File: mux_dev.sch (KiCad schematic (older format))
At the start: 3 parts, among them U10 FSUSB42MUX, U11 FSUSB42MUX, U9 FSUSB42MUX

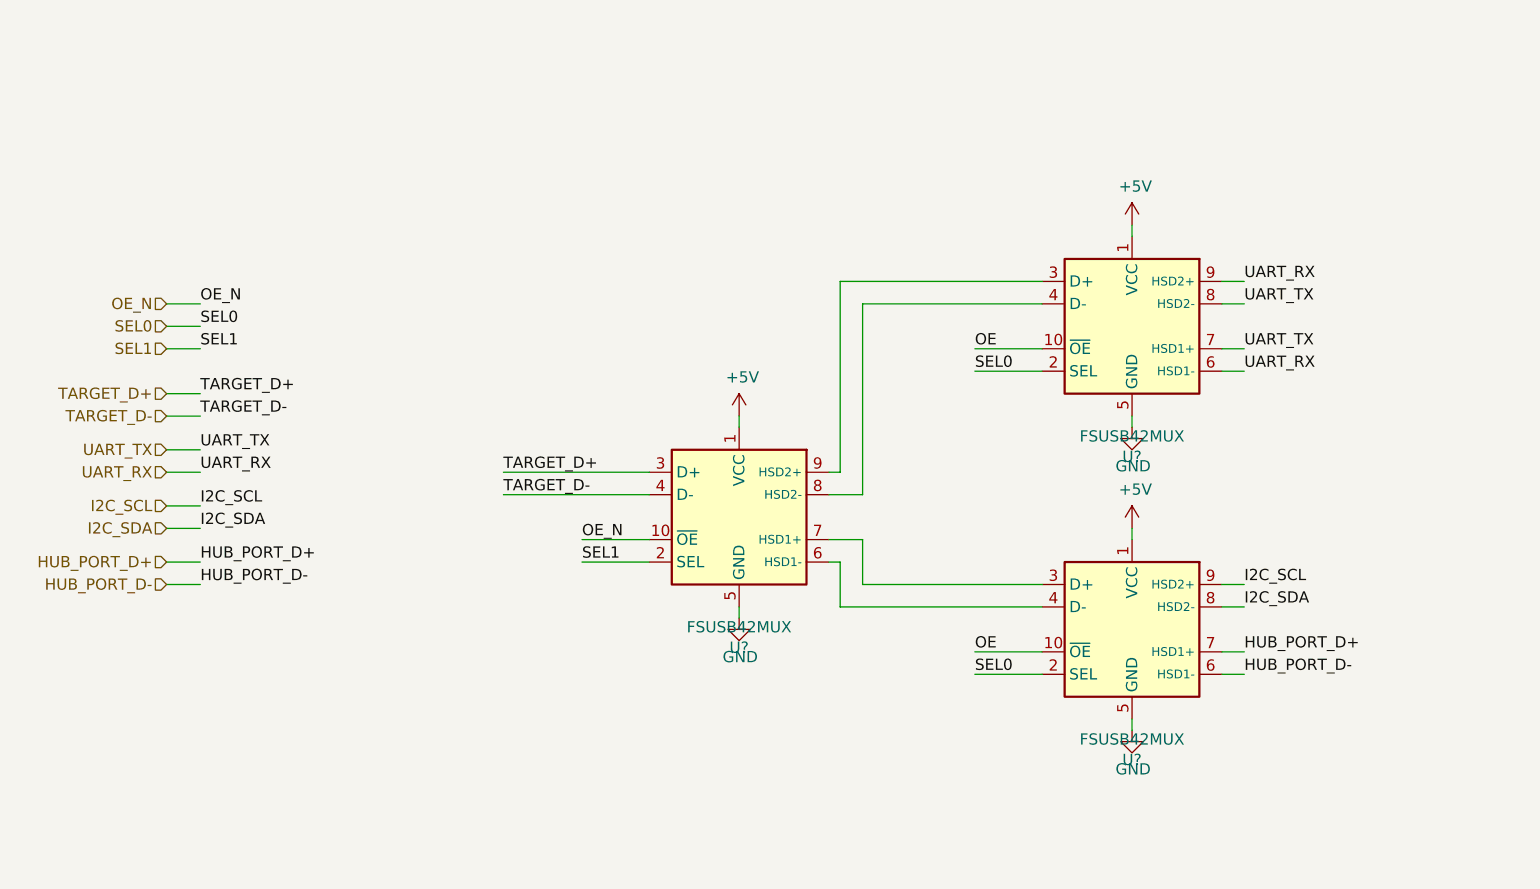
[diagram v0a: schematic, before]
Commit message: Complete muxing and level translation
Added Aux USB to avoid using a HUB, which don't seem to be too readily
available out there and would complicate the design for no good reason.

Now the i2c lines can also be switched.

Added voltage level translation up to 1.2V from 3.3V. Selected
bidirectional level translator.

Started looking into power supply.
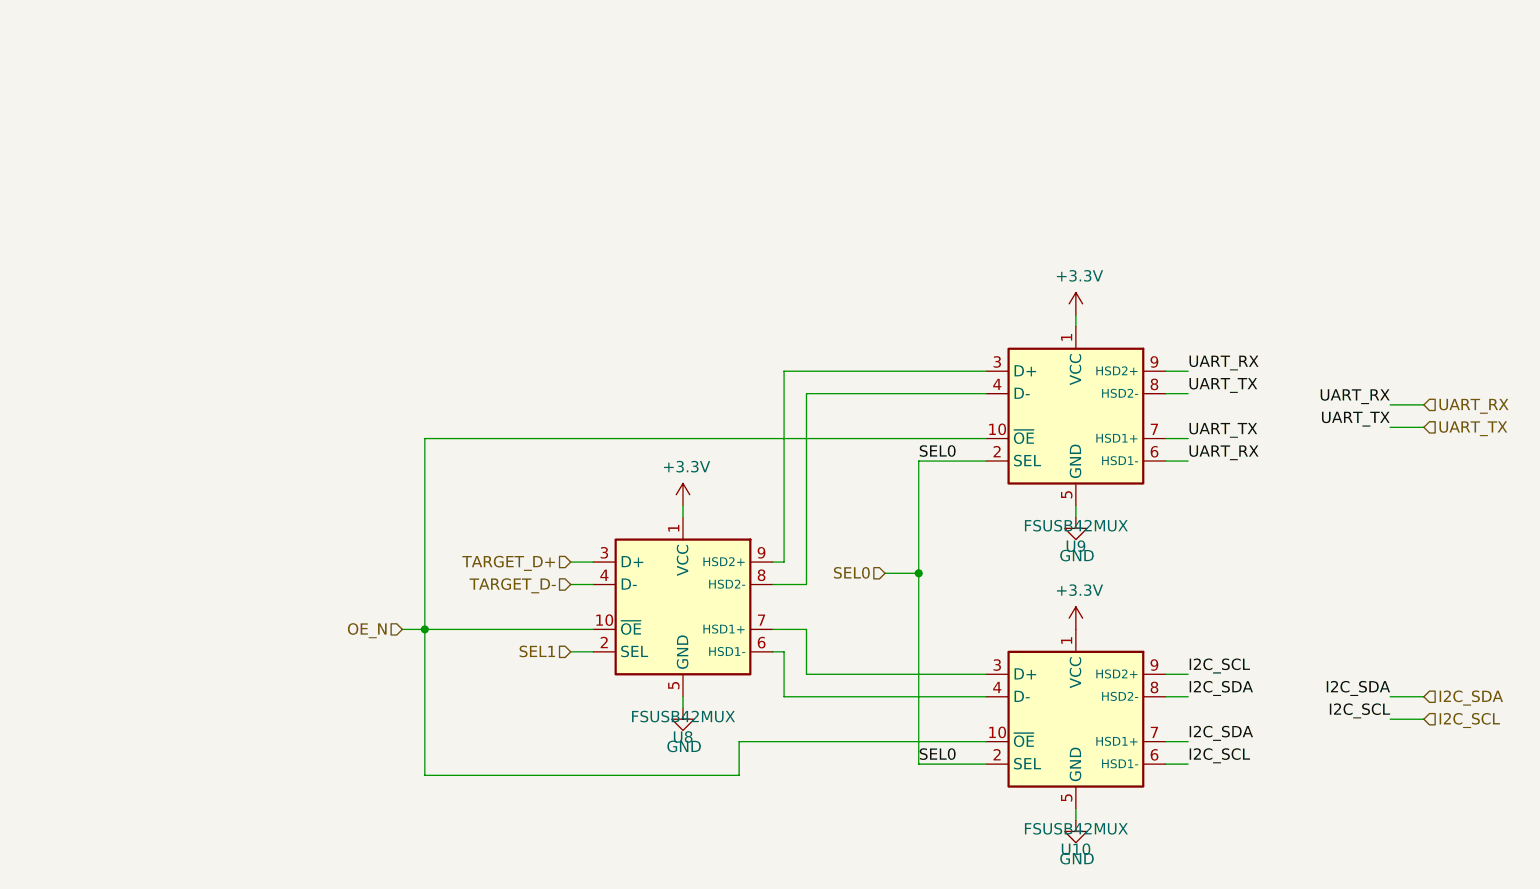
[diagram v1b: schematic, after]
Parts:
- renumbered U9 to U14, U10 to U15, U11 to U16
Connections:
- net HUB_PORT_D+ is gone; now on net I2C_SDA: U16.7 (HSD1+)
- net HUB_PORT_D- is gone; now on net I2C_SCL: U16.6 (HSD1-)
- net OE is gone; now on net OE_N: U15.10 (~OE), U16.10 (~OE)
- net +5V renamed +3V3
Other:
- moved on the sheet: U10, U8, U9

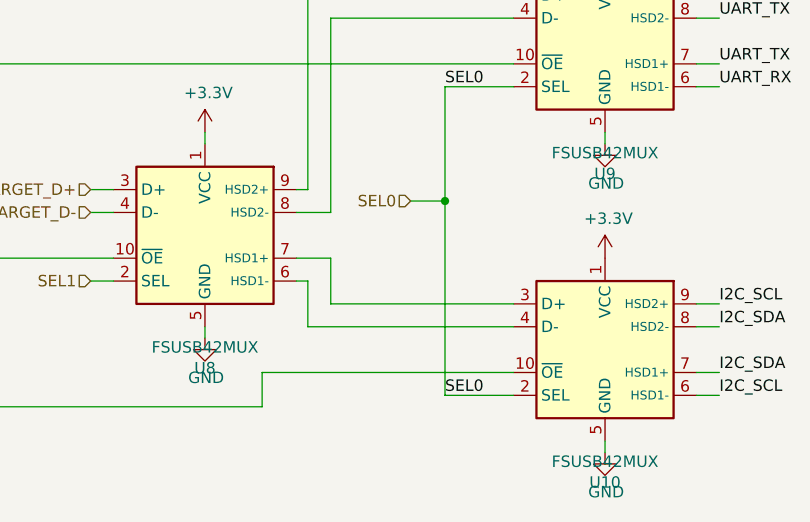
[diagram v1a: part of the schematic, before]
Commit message: Add initial power design
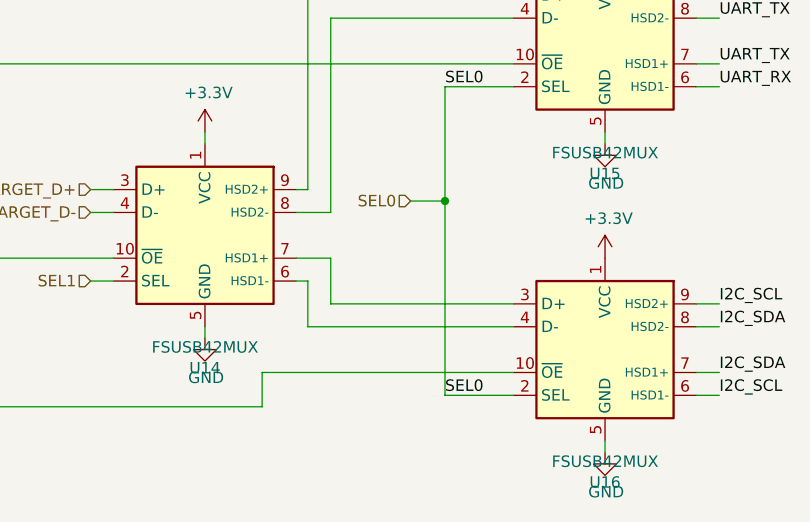
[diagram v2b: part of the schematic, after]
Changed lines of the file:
@@
 AR Path="/61BE2A8A/61D663B4/61D34F4E" Ref="U8"  Part="1"
 AR Path="/61BE2A8A/61D84977/61D34F4E" Ref="U11"  Part="1"
-F 0 "U8" H 4750 3419 50  0000 C CNN
+F 0 "U14" H 4750 3419 50  0000 C CNN
 F 1 "FSUSB42MUX" H 4750 3510 50  0000 C CNN
 F 2 "Package_SO:MSOP-10_3x3mm_P0.5mm" H 4750 3200 50  0001 C CNN
@@
 AR Path="/61BE2A8A/61D663B4/61D34F54" Ref="U10"  Part="1"
 AR Path="/61BE2A8A/61D84977/61D34F54" Ref="U13"  Part="1"
-F 0 "U10" H 6500 3919 50  0000 C CNN
+F 0 "U16" H 6500 3919 50  0000 C CNN
 F 1 "FSUSB42MUX" H 6500 4010 50  0000 C CNN
 F 2 "Package_SO:MSOP-10_3x3mm_P0.5mm" H 6500 3700 50  0001 C CNN
@@
 AR Path="/61BE2A8A/61D663B4/61D34F72" Ref="#PWR020"  Part="1"
 AR Path="/61BE2A8A/61D84977/61D34F72" Ref="#PWR026"  Part="1"
-F 0 "#PWR020" H 6500 3350 50  0001 C CNN
+F 0 "#PWR032" H 6500 3350 50  0001 C CNN
 F 1 "GND" H 6505 3427 50  0000 C CNN
 F 2 "" H 6500 3600 50  0001 C CNN
@@
 AR Path="/61BE2A8A/61D663B4/61D34F78" Ref="#PWR022"  Part="1"
 AR Path="/61BE2A8A/61D84977/61D34F78" Ref="#PWR028"  Part="1"
-F 0 "#PWR022" H 6500 4700 50  0001 C CNN
+F 0 "#PWR034" H 6500 4700 50  0001 C CNN
 F 1 "GND" H 6505 4777 50  0000 C CNN
 F 2 "" H 6500 4950 50  0001 C CNN
@@
 AR Path="/61BE2A8A/61D663B4/61D34F7E" Ref="#PWR018"  Part="1"
 AR Path="/61BE2A8A/61D84977/61D34F7E" Ref="#PWR024"  Part="1"
-F 0 "#PWR018" H 4750 4200 50  0001 C CNN
+F 0 "#PWR030" H 4750 4200 50  0001 C CNN
 F 1 "GND" H 4755 4277 50  0000 C CNN
 F 2 "" H 4750 4450 50  0001 C CNN
@@
 AR Path="/61BE2A8A/61D663B4/61D34F88" Ref="U9"  Part="1"
 AR Path="/61BE2A8A/61D84977/61D34F88" Ref="U12"  Part="1"
-F 0 "U9" H 6500 2569 50  0000 C CNN
+F 0 "U15" H 6500 2569 50  0000 C CNN
 F 1 "FSUSB42MUX" H 6500 2660 50  0000 C CNN
 F 2 "Package_SO:MSOP-10_3x3mm_P0.5mm" H 6500 2350 50  0001 C CNN
@@
 AR Path="/61BE2A8A/61D84977/61C11FA3" Ref="#PWR0104"  Part="1"
 AR Path="/61BE2A8A/61D2FA96/61C11FA3" Ref="#PWR0107"  Part="1"
-F 0 "#PWR0101" H 6500 2550 50  0001 C CNN
+F 0 "#PWR0107" H 6500 2550 50  0001 C CNN
 F 1 "+3.3V" H 6515 2873 50  0000 C CNN
 F 2 "" H 6500 2700 50  0001 C CNN
@@
 AR Path="/61BE2A8A/61D84977/61C140A7" Ref="#PWR0105"  Part="1"
 AR Path="/61BE2A8A/61D2FA96/61C140A7" Ref="#PWR0108"  Part="1"
-F 0 "#PWR0102" H 6500 3950 50  0001 C CNN
+F 0 "#PWR0108" H 6500 3950 50  0001 C CNN
 F 1 "+3.3V" H 6515 4273 50  0000 C CNN
 F 2 "" H 6500 4100 50  0001 C CNN
@@
 AR Path="/61BE2A8A/61D84977/61C14C77" Ref="#PWR0106"  Part="1"
 AR Path="/61BE2A8A/61D2FA96/61C14C77" Ref="#PWR0109"  Part="1"
-F 0 "#PWR0103" H 4750 3400 50  0001 C CNN
+F 0 "#PWR0109" H 4750 3400 50  0001 C CNN
 F 1 "+3.3V" H 4765 3723 50  0000 C CNN
 F 2 "" H 4750 3550 50  0001 C CNN

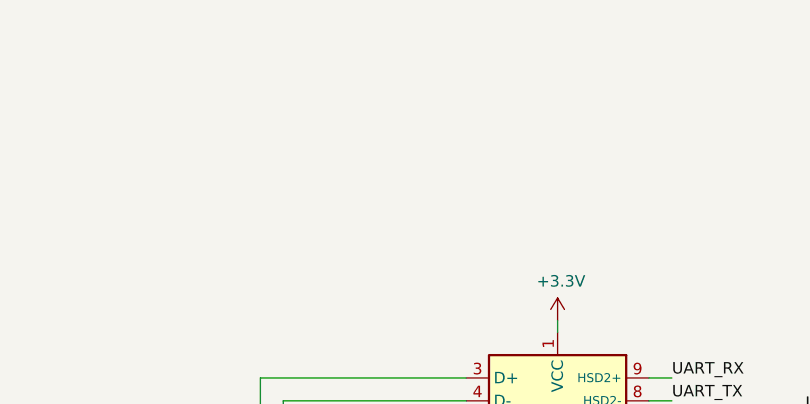
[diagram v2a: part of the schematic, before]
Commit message: Supply caps, initial signal states and headers
  * Added bulk supply caps.
  * Set initial control signal states via resistors.
  * Add debug headers.
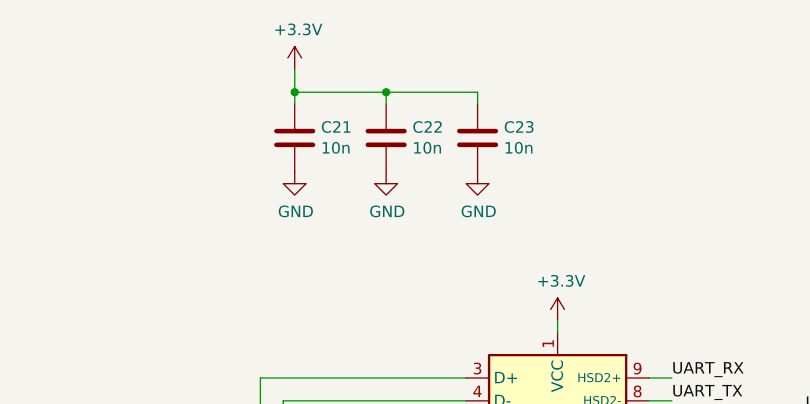
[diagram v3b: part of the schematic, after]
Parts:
- added C15, C16, C17: 10n, symbol Device:C
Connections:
- net +3V3: now also C15.1, C16.1, C17.1
- net GND: now also C15.2, C16.2, C17.2
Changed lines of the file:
@@
 $Descr A4 11693 8268
 encoding utf-8
-Sheet 5 12
+Sheet 7 12
 Title ""
 Date ""
@@
 	1    0    0    -1
 $EndComp
+$Comp
+L Device:C C15
+U 1 1 61B68F9B
+P 5350 1900
+AR Path="/61BE2A8A/61D663B4/61B68F9B" Ref="C15"  Part="1"
+AR Path="/61BE2A8A/61D84977/61B68F9B" Ref="C18"  Part="1"
+AR Path="/61BE2A8A/61D2FA96/61B68F9B" Ref="C21"  Part="1"
+F 0 "C21" H 5465 1946 50  0000 L CNN
+F 1 "10n" H 5465 1855 50  0000 L CNN
+F 2 "" H 5388 1750 50  0001 C CNN
+F 3 "~" H 5350 1900 50  0001 C CNN
+	1    5350 1900
+	1    0    0    -1
+$EndComp
+$Comp
+L power:GND #PWR0134
+U 1 1 61B68FA1
+P 5350 2050
+AR Path="/61BE2A8A/61D663B4/61B68FA1" Ref="#PWR0134"  Part="1"
+AR Path="/61BE2A8A/61D84977/61B68FA1" Ref="#PWR0138"  Part="1"
+AR Path="/61BE2A8A/61D2FA96/61B68FA1" Ref="#PWR0142"  Part="1"
+F 0 "#PWR0142" H 5350 1800 50  0001 C CNN
+F 1 "GND" H 5355 1877 50  0000 C CNN
+F 2 "" H 5350 2050 50  0001 C CNN
+F 3 "" H 5350 2050 50  0001 C CNN
+	1    5350 2050
+	1    0    0    -1
+$EndComp
+$Comp
+L power:+3.3V #PWR0135
+U 1 1 61B68FA7
+P 5350 1600
+AR Path="/61BE2A8A/61D663B4/61B68FA7" Ref="#PWR0135"  Part="1"
+AR Path="/61BE2A8A/61D84977/61B68FA7" Ref="#PWR0139"  Part="1"
+AR Path="/61BE2A8A/61D2FA96/61B68FA7" Ref="#PWR0143"  Part="1"
+F 0 "#PWR0143" H 5350 1450 50  0001 C CNN
+F 1 "+3.3V" H 5365 1773 50  0000 C CNN
+F 2 "" H 5350 1600 50  0001 C CNN
+F 3 "" H 5350 1600 50  0001 C CNN
+	1    5350 1600
+	1    0    0    -1
+$EndComp
+$Comp
+L Device:C C16
+U 1 1 61B68FAD
+P 5750 1900
+AR Path="/61BE2A8A/61D663B4/61B68FAD" Ref="C16"  Part="1"
+AR Path="/61BE2A8A/61D84977/61B68FAD" Ref="C19"  Part="1"
+AR Path="/61BE2A8A/61D2FA96/61B68FAD" Ref="C22"  Part="1"
+F 0 "C22" H 5865 1946 50  0000 L CNN
+F 1 "10n" H 5865 1855 50  0000 L CNN
+F 2 "" H 5788 1750 50  0001 C CNN
+F 3 "~" H 5750 1900 50  0001 C CNN
+	1    5750 1900
+	1    0    0    -1
+$EndComp
+$Comp
+L power:GND #PWR0136
+U 1 1 61B68FB3
+P 5750 2050
+AR Path="/61BE2A8A/61D663B4/61B68FB3" Ref="#PWR0136"  Part="1"
+AR Path="/61BE2A8A/61D84977/61B68FB3" Ref="#PWR0140"  Part="1"
+AR Path="/61BE2A8A/61D2FA96/61B68FB3" Ref="#PWR0144"  Part="1"
+F 0 "#PWR0144" H 5750 1800 50  0001 C CNN
+F 1 "GND" H 5755 1877 50  0000 C CNN
+F 2 "" H 5750 2050 50  0001 C CNN
+F 3 "" H 5750 2050 50  0001 C CNN
+	1    5750 2050
+	1    0    0    -1
+$EndComp
+$Comp
+L Device:C C17
+U 1 1 61B68FB9
+P 6150 1900
+AR Path="/61BE2A8A/61D663B4/61B68FB9" Ref="C17"  Part="1"
+AR Path="/61BE2A8A/61D84977/61B68FB9" Ref="C20"  Part="1"
+AR Path="/61BE2A8A/61D2FA96/61B68FB9" Ref="C23"  Part="1"
+F 0 "C23" H 6265 1946 50  0000 L CNN
+F 1 "10n" H 6265 1855 50  0000 L CNN
+F 2 "" H 6188 1750 50  0001 C CNN
+F 3 "~" H 6150 1900 50  0001 C CNN
+	1    6150 1900
+	1    0    0    -1
+$EndComp
+$Comp
+L power:GND #PWR0137
+U 1 1 61B68FBF
+P 6150 2050
+AR Path="/61BE2A8A/61D663B4/61B68FBF" Ref="#PWR0137"  Part="1"
+AR Path="/61BE2A8A/61D84977/61B68FBF" Ref="#PWR0141"  Part="1"
+AR Path="/61BE2A8A/61D2FA96/61B68FBF" Ref="#PWR0145"  Part="1"
+F 0 "#PWR0145" H 6150 1800 50  0001 C CNN
+F 1 "GND" H 6155 1877 50  0000 C CNN
+F 2 "" H 6150 2050 50  0001 C CNN
+F 3 "" H 6150 2050 50  0001 C CNN
+	1    6150 2050
+	1    0    0    -1
+$EndComp
+Wire Wire Line
+	5350 1700 5350 1600
+Wire Wire Line
+	5350 1700 5350 1750
+Connection ~ 5350 1700
+Wire Wire Line
+	5750 1700 5750 1750
+Connection ~ 5750 1700
+Wire Wire Line
+	5750 1700 5350 1700
+Wire Wire Line
+	6150 1700 6150 1750
+Wire Wire Line
+	6150 1700 5750 1700
 $EndSCHEMATC
